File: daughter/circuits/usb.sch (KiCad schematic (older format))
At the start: 15 parts, among them J11 USB_MINI_B, J12 Conn_02x02_Counter_Clockwise, Q17 Q_NPN, Q18 Q_PNP, U16 FT231XS

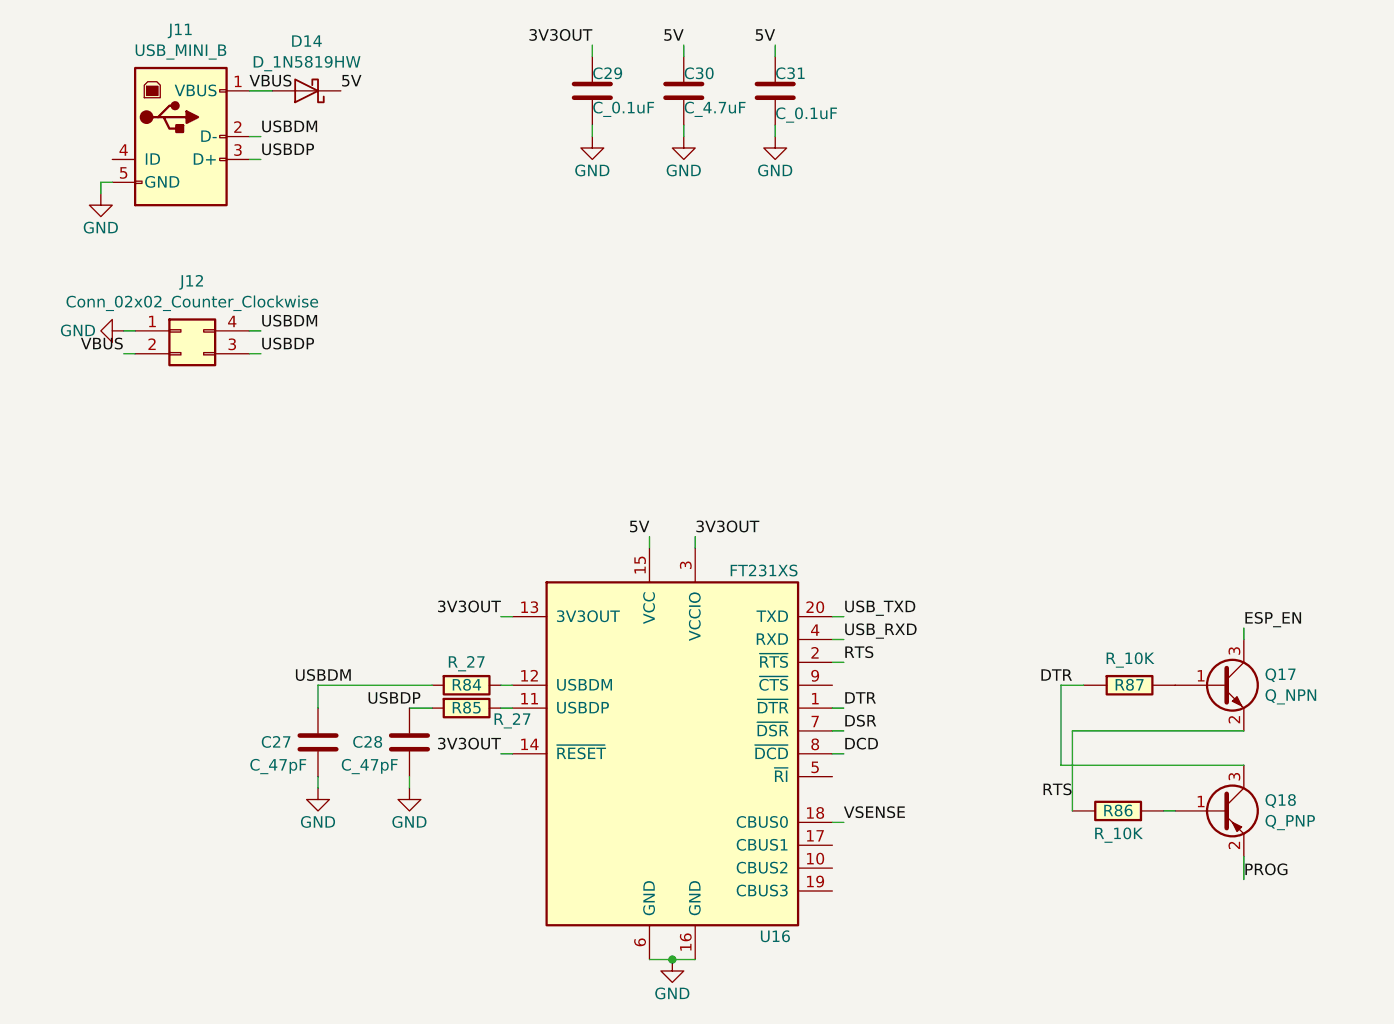
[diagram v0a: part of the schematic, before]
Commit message: 0) Switched to h-bridge drivers for hvac 1) Connected ignition sense io 2) MCP config pins and reset 3) Fixed usb resistors 4) Fixed BJT footprint 5) Added car interface pcb for C6 Corvette
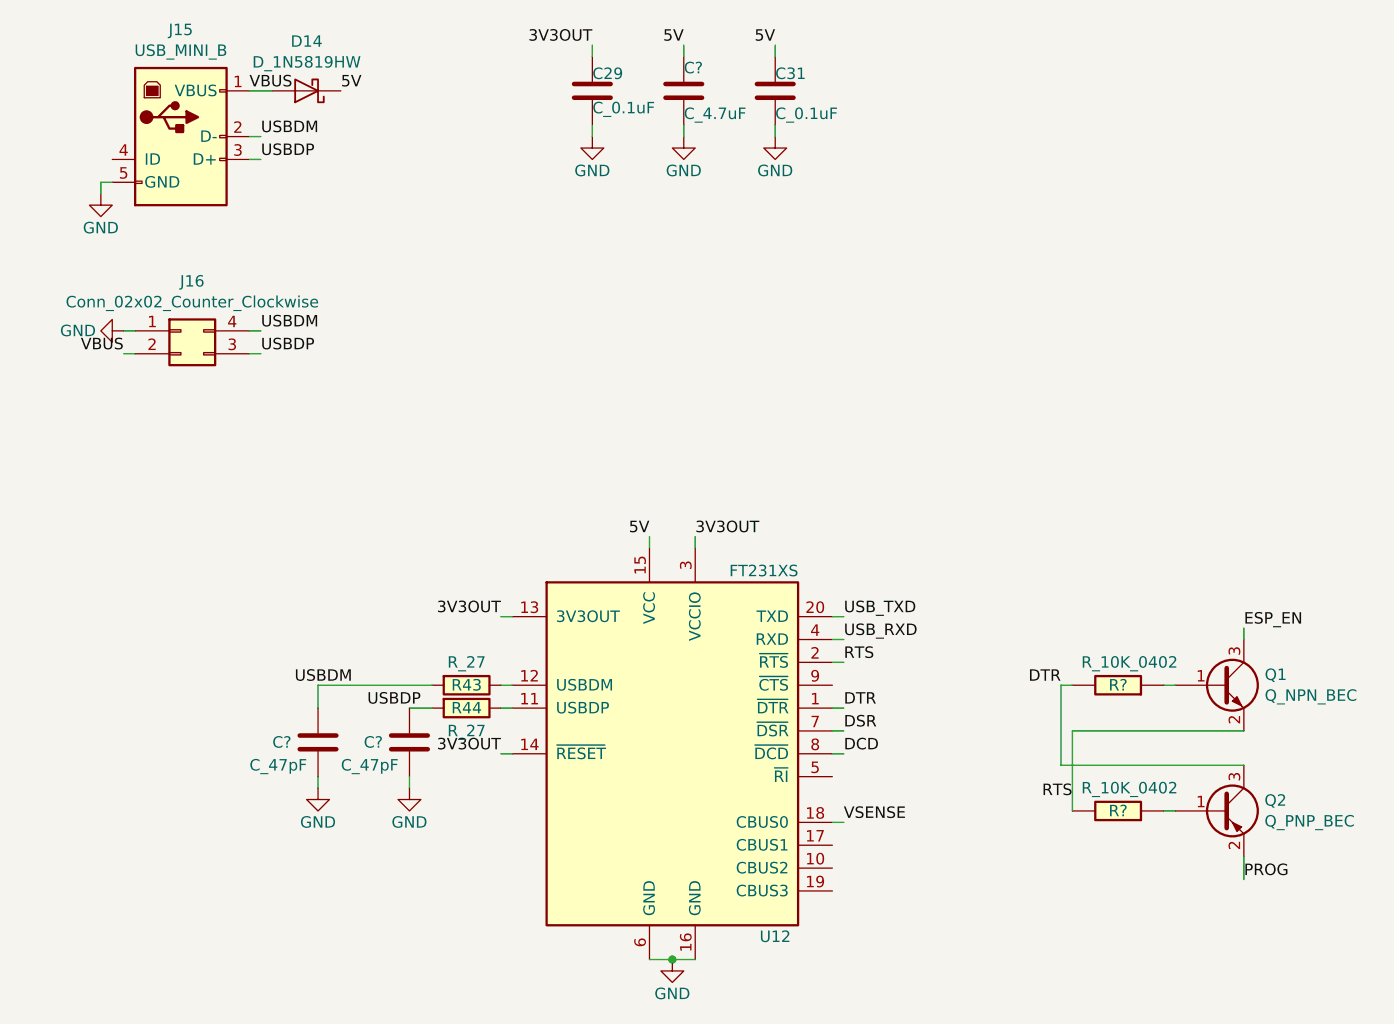
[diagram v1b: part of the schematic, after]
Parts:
- removed C27, C28: C_47pF, Capacitor_SMD:C_0603_1608Metric_Pad1.08x0.95mm_HandSolder, symbol open-dash-daughterboard-rescue:C_47pF-Open_Automation
- removed C30: C_4.7uF, Capacitor_SMD:C_0603_1608Metric_Pad1.08x0.95mm_HandSolder, symbol open-dash-daughterboard-rescue:C_4.7uF-Open_Automation
- removed Q17: Q_NPN, Package_TO_SOT_SMD:SOT-23, symbol open-dash-daughterboard-rescue:Q_NPN-Open_Automation
- removed Q18: Q_PNP, Package_TO_SOT_SMD:SOT-23, symbol open-dash-daughterboard-rescue:Q_PNP-Open_Automation
- removed R84, R85: R_27, Resistor_SMD:R_0603_1608Metric_Pad0.98x0.95mm_HandSolder, symbol open-dash-daughterboard-rescue:R_27-Open_Automation
- removed R86, R87: R_10K, Resistor_SMD:R_0603_1608Metric_Pad0.98x0.95mm_HandSolder, symbol open-dash-daughterboard-rescue:R_10K-Open_Automation
- added C? (x2): C_47pF, Capacitor_SMD:C_0603_1608Metric_Pad1.08x0.95mm_HandSolder, symbol Open_Automation:C_47pF
- added C?: C_4.7uF, Capacitor_SMD:C_0805_2012Metric_Pad1.18x1.45mm_HandSolder, symbol Open_Automation:C_4.7uF
- added Q1: Q_NPN_BEC, Package_TO_SOT_SMD:SOT-23, symbol Open_Automation:Q_NPN_BEC
- added Q2: Q_PNP_BEC, Package_TO_SOT_SMD:SOT-23, symbol Open_Automation:Q_PNP_BEC
- added R43, R44: R_27, Resistor_SMD:R_0603_1608Metric_Pad0.98x0.95mm_HandSolder, symbol Open_Automation:R_27
- added R? (x2): R_10K_0402, Resistor_SMD:R_0402_1005Metric_Pad0.72x0.64mm_HandSolder, symbol Open_Automation:R_10K_0402
- renumbered J11 to J15, J12 to J16, U16 to U12
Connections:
- net 5V: now also C?.1
- net DTR: now also Q2.3 (C), R?.2
- net ESP_EN: now also Q1.3 (C)
- net GND: now also C?.2, C?.2, C?.2
- net PROG: now also Q2.2 (E)
- net RTS: now also Q1.2 (E), R?.2
- net USBDM: now also C?.1, R43.2
- net USBDP: now also C?.1, R44.2
- net at U12.12 (USBDM): now also R43.1
- net at U12.11 (USBDP): now also R44.1
- new net: Q1.1 (B), R?.1
- new net: Q2.1 (B), R?.1

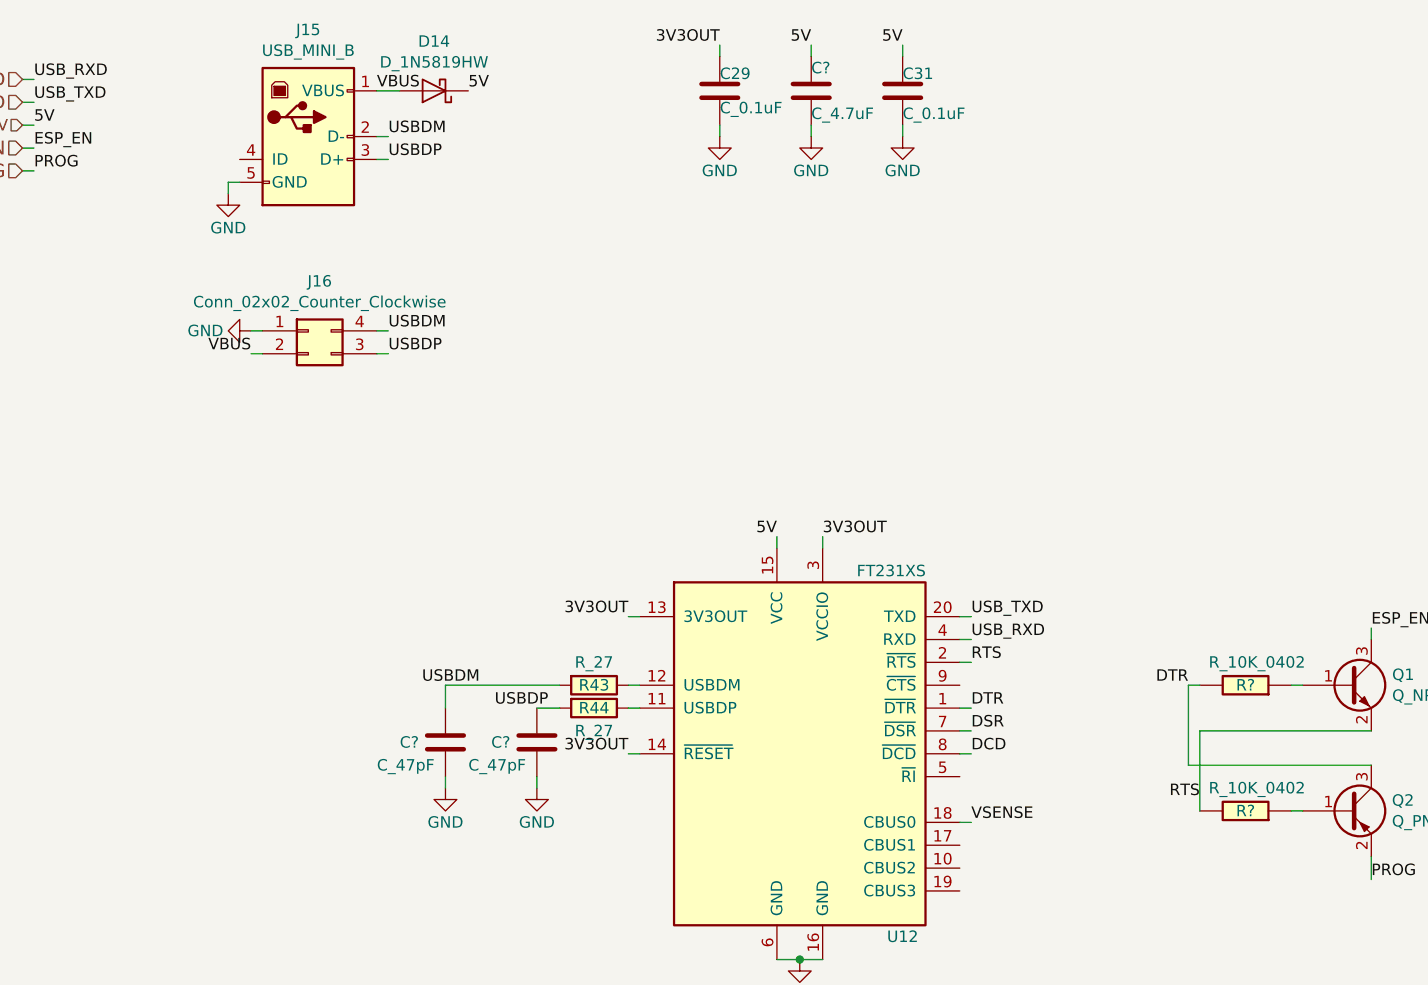
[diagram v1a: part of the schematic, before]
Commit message: finished schematic, working on layout
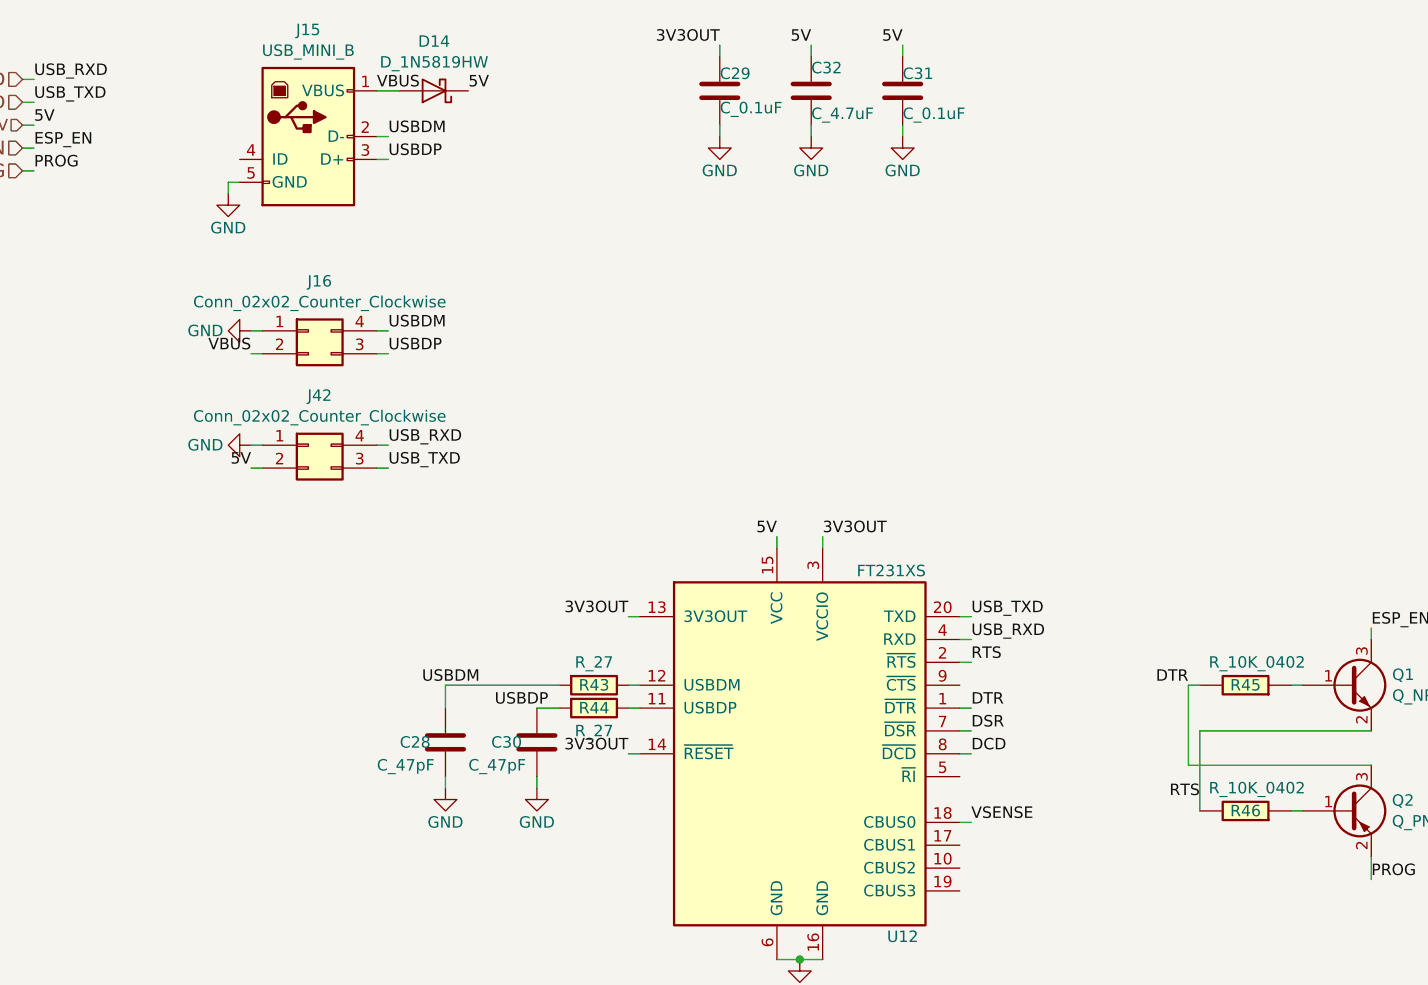
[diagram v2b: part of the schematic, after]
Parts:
- added J42: Conn_02x02_Counter_Clockwise, Connector_PinHeader_2.54mm:PinHeader_2x02_P2.54mm_Vertical, symbol open-dash-daughterboard-rescue:Conn_02x02_Counter_Clockwise-Connector_Generic
- gave numbers to parts that had none: 5
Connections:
- net 5V: now also J42.2 (Pin_2)
- net GND: now also J42.1 (Pin_1)
- net RXD: now also J42.3 (Pin_3)
- net TXD: now also J42.4 (Pin_4)
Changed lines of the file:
@@
 $EndComp
 $Comp
-L Open_Automation:R_10K_0402 R?
+L Open_Automation:R_10K_0402 R45
 U 1 1 60498F5F
 P 6700 3700
-F 0 "R?" V 6700 3700 50  0000 C CNN
+F 0 "R45" V 6700 3700 50  0000 C CNN
 F 1 "R_10K_0402" V 6800 3650 50  0000 C CNN
 F 2 "Resistor_SMD:R_0402_1005Metric_Pad0.72x0.64mm_HandSolder" V 6630 3700 50  0001 C CNN
@@
 $EndComp
 $Comp
-L Open_Automation:R_10K_0402 R?
+L Open_Automation:R_10K_0402 R46
 U 1 1 6049BC20
 P 6700 4250
-F 0 "R?" V 6700 4250 50  0000 C CNN
+F 0 "R46" V 6700 4250 50  0000 C CNN
 F 1 "R_10K_0402" V 6800 4200 50  0000 C CNN
 F 2 "Resistor_SMD:R_0402_1005Metric_Pad0.72x0.64mm_HandSolder" V 6630 4250 50  0001 C CNN
@@
 	6450 3700 6500 3700
 $Comp
-L Open_Automation:C_47pF C?
+L Open_Automation:C_47pF C30
 U 1 1 604AA3C1
 P 3600 3950
-F 0 "C?" H 3400 3950 50  0000 L CNN
+F 0 "C30" H 3400 3950 50  0000 L CNN
 F 1 "C_47pF" H 3300 3850 50  0000 L CNN
 F 2 "Capacitor_SMD:C_0603_1608Metric_Pad1.08x0.95mm_HandSolder" H 3700 4250 50  0001 C CNN
@@
 $EndComp
 $Comp
-L Open_Automation:C_47pF C?
+L Open_Automation:C_47pF C28
 U 1 1 604ABFFB
 P 3200 3950
-F 0 "C?" H 3000 3950 50  0000 L CNN
+F 0 "C28" H 3000 3950 50  0000 L CNN
 F 1 "C_47pF" H 2900 3850 50  0000 L CNN
 F 2 "Capacitor_SMD:C_0603_1608Metric_Pad1.08x0.95mm_HandSolder" H 3300 4250 50  0001 C CNN
@@
 $EndComp
 $Comp
-L Open_Automation:C_4.7uF C?
+L Open_Automation:C_4.7uF C32
 U 1 1 604B5BCC
 P 4800 1100
-F 0 "C?" H 4800 1200 50  0000 L CNN
+F 0 "C32" H 4800 1200 50  0000 L CNN
 F 1 "C_4.7uF" H 4800 1000 50  0000 L CNN
 F 2 "Capacitor_SMD:C_0805_2012Metric_Pad1.18x1.45mm_HandSolder" H 4900 1400 50  0001 C CNN
@@
 	1    0    0    -1
 $EndComp
+$Comp
+L open-dash-daughterboard-rescue:Conn_02x02_Counter_Clockwise-Connector_Generic J42
+U 1 1 60569BF3
+P 2600 2650
+F 0 "J42" H 2650 2867 50  0000 C CNN
+F 1 "Conn_02x02_Counter_Clockwise" H 2650 2776 50  0000 C CNN
+F 2 "Connector_PinHeader_2.54mm:PinHeader_2x02_P2.54mm_Vertical" H 2600 2650 50  0001 C CNN
+F 3 "~" H 2600 2650 50  0001 C CNN
+	1    2600 2650
+	1    0    0    -1
+$EndComp
+$Comp
+L open-dash-daughterboard-rescue:GND-power #PWR?
+U 1 1 60569D73
+P 2350 2650
+AR Path="/5ABD187E/60569D73" Ref="#PWR?"  Part="1"
+AR Path="/60569D73" Ref="#PWR?"  Part="1"
+AR Path="/5A7BADB8/60569D73" Ref="#PWR?"  Part="1"
+AR Path="/60DDD162/60569D73" Ref="#PWR0173"  Part="1"
+F 0 "#PWR0173" H 2350 2400 50  0001 C CNN
+F 1 "GND" V 2350 2450 50  0000 C CNN
+F 2 "" H 2350 2650 50  0000 C CNN
+F 3 "" H 2350 2650 50  0000 C CNN
+	1    2350 2650
+	0    1    1    0
+$EndComp
+Wire Wire Line
+	2350 2650 2400 2650
+Wire Wire Line
+	2350 2750 2400 2750
+Wire Wire Line
+	2900 2750 2950 2750
+Wire Wire Line
+	2950 2650 2900 2650
+Text Label 2350 2750 2    50   ~ 0
+5V
+Text Label 2950 2650 0    50   ~ 0
+USB_RXD
+Text Label 2950 2750 0    50   ~ 0
+USB_TXD
 $EndSCHEMATC

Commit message: finished layout
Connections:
- net RXD: now also J42.4 (Pin_4); no longer J42.3 (Pin_3)
- net TXD: now also J42.3 (Pin_3); no longer J42.4 (Pin_4)
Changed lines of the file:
@@
 	2350 2750 2400 2750
 Wire Wire Line
-	2900 2750 2950 2750
+	2900 2650 2950 2650
 Wire Wire Line
-	2950 2650 2900 2650
+	2950 2750 2900 2750
 Text Label 2350 2750 2    50   ~ 0
 5V
+Text Label 2950 2750 0    50   ~ 0
+USB_RXD
 Text Label 2950 2650 0    50   ~ 0
-USB_RXD
-Text Label 2950 2750 0    50   ~ 0
 USB_TXD
 $EndSCHEMATC

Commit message: sent v1.2 to fab
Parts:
- removed D14: D_1N5819HW, Diode_SMD:D_SOD-123, symbol open-dash-daughterboard-rescue:D_1N5819HW-Open_Automation
- added D14: D_1N5819HW, Diode_SMD:D_SOD-123, symbol Open_Automation:D_1N5819HW
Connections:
- net 5V: now also D14.1 (K)
- net VBUS: now also D14.2 (A)
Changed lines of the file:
@@
 5V
-$Comp
-L open-dash-daughterboard-rescue:D_1N5819HW-Open_Automation D?
-U 1 1 5CD8937E
-P 3150 1100
-AR Path="/5B15E02A/5CD8937E" Ref="D?"  Part="1"
-AR Path="/60DDD162/5CD8937E" Ref="D14"  Part="1"
-F 0 "D14" H 3150 884 50  0000 C CNN
-F 1 "D_1N5819HW" H 3150 975 50  0000 C CNN
-F 2 "Diode_SMD:D_SOD-123" H 3150 925 50  0001 C CNN
-F 3 "http://www.diodes.com/_files/datasheets/ds23022.pdf" H 3150 1100 50  0001 C CNN
-F 4 "1N5819HW-7-F" H 3150 1400 50  0001 C CNN "Part Number"
-F 5 "https://www.digikey.com/product-detail/en/diodes-incorporated/1N5819HW-7-F/1N5819HW-FDICT-ND/815283" H 3250 1300 50  0001 C CNN "Website"
-F 6 "C117948" H 50  0   50  0001 C CNN "LCSC"
-	1    3150 1100
-	-1   0    0    1
-$EndComp
 $Comp
 L open-dash-daughterboard-rescue:GND-power #PWR?
@@
 Text Label 2950 2650 0    50   ~ 0
 USB_TXD
+$Comp
+L Open_Automation:D_1N5819HW D?
+U 1 1 60770B3C
+P 3150 1100
+AR Path="/6063934A/60770B3C" Ref="D?"  Part="1"
+AR Path="/60DDD162/60770B3C" Ref="D14"  Part="1"
+F 0 "D14" H 3150 1000 50  0000 C CNN
+F 1 "D_1N5819HW" H 2800 1150 50  0000 C CNN
+F 2 "Diode_SMD:D_SOD-123" H 3150 925 50  0001 C CNN
+F 3 "https://datasheet.lcsc.com/szlcsc/Diodes-Incorporated-1N5819HW-7-F_C82544.pdf" H 3150 1100 50  0001 C CNN
+F 4 "1N5819HW-7-F" H 3150 1400 50  0001 C CNN "Part Number"
+F 5 "C82544" H 3150 1500 50  0001 C CNN "LCSC"
+	1    3150 1100
+	-1   0    0    1
+$EndComp
 $EndSCHEMATC

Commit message: update
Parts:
- added C10: C_100nF_0402, Capacitor_SMD:C_0402_1005Metric_Pad0.74x0.62mm_HandSolder, symbol Open_Automation:C_100nF_0402
- added C7, C8: C_27pF_0402, Capacitor_SMD:C_0402_1005Metric_Pad0.74x0.62mm_HandSolder, symbol Open_Automation:C_27pF_0402
- added C9: C_22uF, Capacitor_SMD:C_0603_1608Metric_Pad1.08x0.95mm_HandSolder, symbol Open_Automation:C_22uF
- added J18: USB_MINI_B, Open_Automation:USB-mini-B-0548190519, symbol Open_Automation:USB_MINI_B
- added Q5: Crystal_12Mhz, Crystal:Crystal_SMD_3225-4Pin_3.2x2.5mm_HandSoldering, symbol Open_Automation:Crystal_12Mhz
- added Q6: Q_SS8050, Package_TO_SOT_SMD:SOT-23, symbol Open_Automation:Q_SS8050
- added Q7: Q_SS8550, Package_TO_SOT_SMD:SOT-23, symbol Open_Automation:Q_SS8550
- added R41, R42, R46: R_10K_0402, Resistor_SMD:R_0402_1005Metric_Pad0.72x0.64mm_HandSolder, symbol Open_Automation:R_10K_0402
- added R43, R44: R_1K_0402, Resistor_SMD:R_0402_1005Metric_Pad0.72x0.64mm_HandSolder, symbol Open_Automation:R_1K_0402
- added U10: CH340T(SSOP20W), Open_Automation:SSOP-20W, symbol Open_Automation:CH340T(SSOP20W)
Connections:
- net TXD is gone; now on net RXD: J42.3 (Pin_3), U12.4 (RXD)
- net 5V: now also C9.1, J18.1 (VBUS), R41.1, U10.19 (VCC)
- net ESP_EN: now also Q6.3 (C)
- net GND: now also C10.2, C7.2, C8.2, C9.2, J18.5 (GND), Q5.2 (case), Q5.4 (case), U10.8 (GND)
- net PROG: now also Q7.2 (E)
- net RXD: now also R41.2, R42.2, R46.1, U10.3 (TXD), U10.4 (RXD)
- new net: C10.1, R42.1, U10.5 (V3)
- new net: C7.1, Q5.1, U10.9 (XI)
- new net: C8.1, Q5.3, U10.10 (XO)
- new net: Q7.1 (B), R44.1
- new net: Q6.2 (E), R44.2, U10.16 (RTS#)
- new net: Q6.1 (B), R43.1
- new net: Q7.3 (C), R43.2, U10.15 (DTR#)
- new net +3V3: R46.2
- new net D+: J18.3 (D+), U10.6 (UD+)
- new net D-: J18.2 (D-), U10.7 (UD-)
- no-connect marks 0 -> 6
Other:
- note added: "!!!WARNING!!!\nWhen the board is powered via PoE, don't include the USB cable for to programming it!!!\nIn case this is required, USB-ISO must be used for to guarantee galvanic isolation!\nSee: https://www.olimex.com/Products/USB-Modules/USB-ISO/"
- note added: "0"
- note added: "1"
- note added: "Auto program\n"
- note added: "DTR RTS->EN IO0"
- moved on the sheet: C28, C29, C30, C31, C32, D14, J15, J16, J42, Q1, Q2, R43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
